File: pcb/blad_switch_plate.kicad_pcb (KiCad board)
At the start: 2 copper layers, 228.6 x 76.2 mm, 4 parts

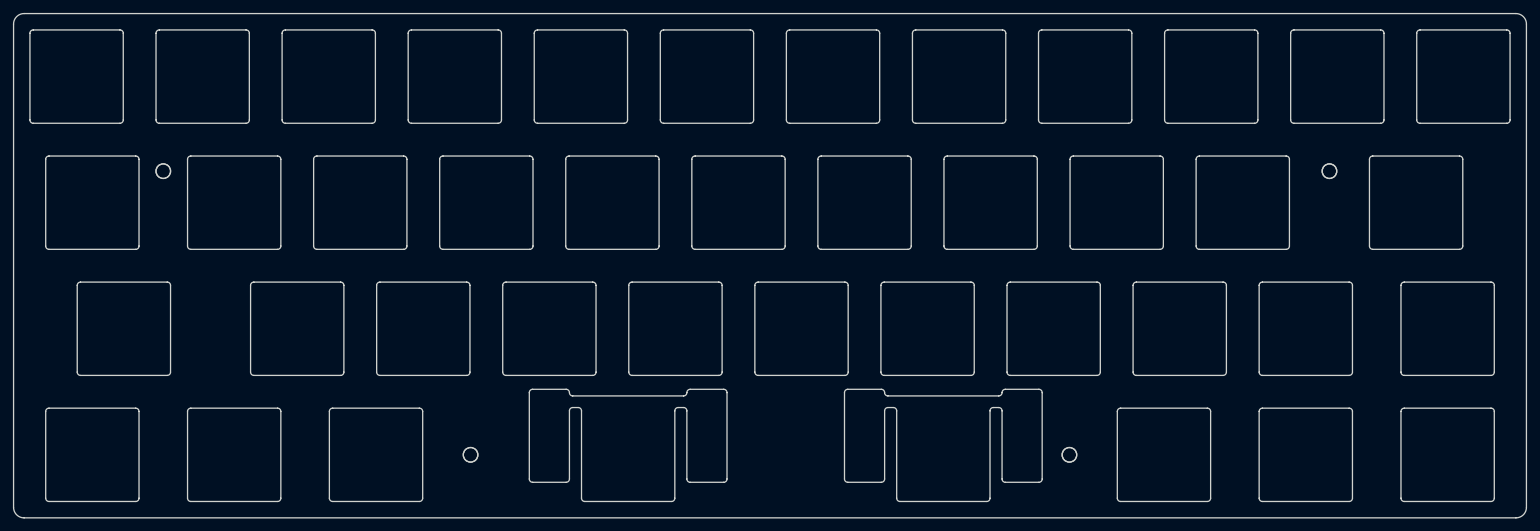
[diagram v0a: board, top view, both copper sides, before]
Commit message: Update PCB and plate designs
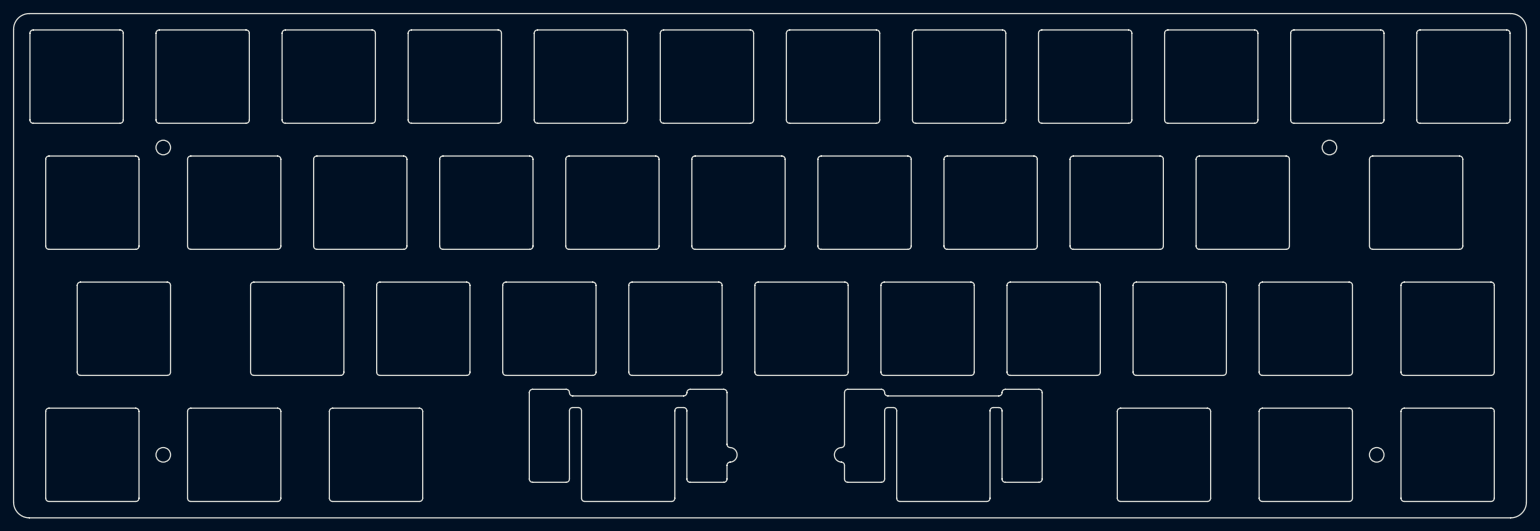
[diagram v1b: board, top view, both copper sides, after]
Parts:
- moved REF** 46.4 mm to (215.5, 85.7)
- moved REF** 46.4 mm to (32.1, 85.7)
- moved REF** 3.57 mm to (208.4, 39.3)
- moved REF** 3.57 mm to (32.1, 39.3)
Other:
- outline, holes or cut-outs redrawn
